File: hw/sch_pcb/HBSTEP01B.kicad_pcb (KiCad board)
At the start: 2 copper layers, 50.3 x 40.1 mm, 56 parts, among them J1 JUMP_2x1, J10 JUMP_2x1, J11 JUMP_2x1, J12 JUMP_2x1, J13 JUMP_2x1, J14 JUMP_2x1, J15 JUMP_2x1, J18 CONN1_1, J19 CONN1_1, J2 JUMP_2x1, J20 CONN1_1, J21 CONN1_1, J22 CONN1_1, J23 CONN1_1, J24 CONN1_1, J25 CONN1_1, J26 CONN1_1, J27 CONN1_1, J3 JUMP_2x1, J4 CONN1_1, J5 CONN1_1, J6 JUMP_2x1, J7 JUMP_2x1, J8 JUMP_2x1, J9 JUMP_2x1, P1 sroub, P2 sroub, P3 sroub, P4 sroub, U1 L6470

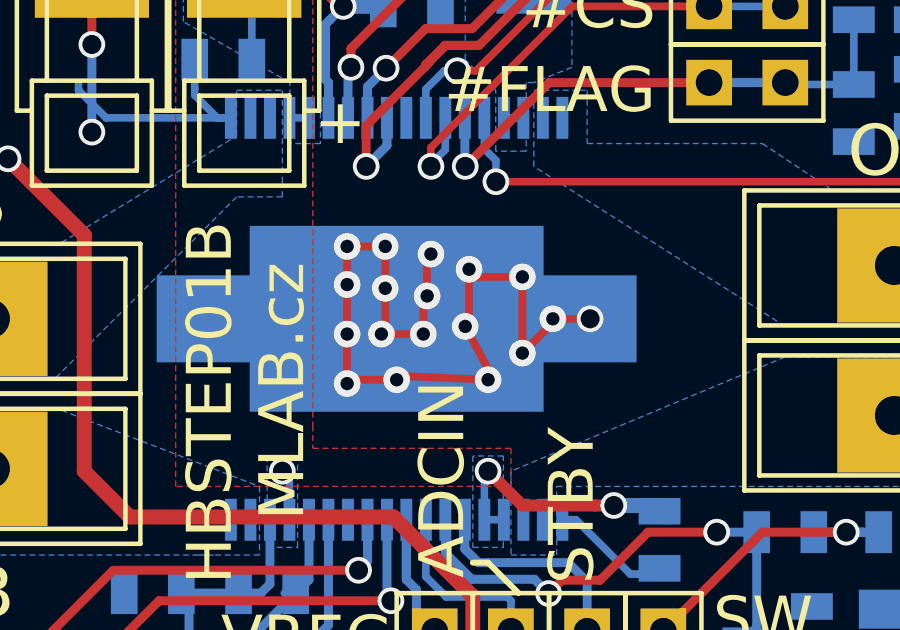
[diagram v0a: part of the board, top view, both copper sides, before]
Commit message: Update project to KiCAD9.
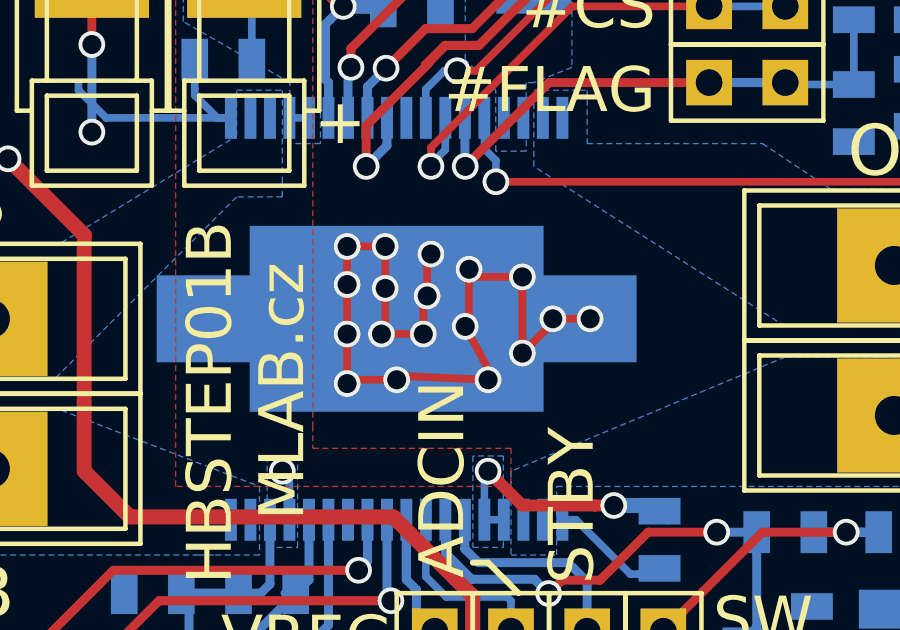
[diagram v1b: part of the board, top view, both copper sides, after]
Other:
- net class Default removed
